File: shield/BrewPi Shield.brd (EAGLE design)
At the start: 53.6 x 59.7 mm, 31 parts, among them J1 ARDUINO_R3_SHIELD_ICSP, U1 SN74HC595N, U2 P-CHANNEL-MOSFET

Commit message: Version 1.2 upload
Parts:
- removed D1, D2: 1N4004, diode:DO41-10
- removed U2: P-CHANNEL-MOSFET, GeekAmmo:SOT23-3
- added Q1: 2N3906, transistor-pnp:TO92
- added R12: 10k Ohm, SparkFun-Passives:AXIAL-0.3
- R10: value 20-30 -> 220; device SparkFun-Passives:AXIAL-0.5 -> SparkFun-Passives:AXIAL-0.3
- R11: value 220 -> 470 Ohm
- RELAY: value 555 -> (none)
- moved R11 59.5 mm to (74.9, 25.4), turned to 270 degrees
- moved R10 56.6 mm to (36.8, 71.1), turned to 180 degrees
- moved R2 1.80 mm to (59.7, 44.5)
- moved R7 0.63 mm to (38.7, 33.0)
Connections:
- removed net N$10: LCD.15, R10.P$1
- removed net N$11: D1.A, U2.3
- removed net N$9: D2.C, R10.P$2
- new net N$7: Q1.1, R11.P$1
- net 5V: now also BTOOTH.4, Q1.3, R10.P$2; no longer BTOOTH.3, R11.P$2
- net A5V: no longer U2.2
- net GND: now also BTOOTH.3; no longer BTOOTH.4
- net N$13: now also R10.P$1; no longer R11.P$1
- net N$2: now also Q1.2, R12.P$2; no longer U1.2, U2.1
- net N$3: now also BTOOTH.1; no longer BTOOTH.2
- net N$5: now also LCD.15, R11.P$2; no longer D1.C, D2.A
- net QB: now also R12.P$1
- net RX: now also BTOOTH.2; no longer BTOOTH.1
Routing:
- net QB: track 10.7 -> 38.9 mm
- net N$9: track 22.3 -> 0.00 mm
- net N$2: track 24.6 -> 9.68 mm
- net A5V: track 60.8 -> 47.6 mm
- net N$11: track 12.0 -> 0.00 mm
- net 5V: track 175.0 -> 184.4 mm
- net N$10: track 9.20 -> 0.00 mm
- net RX: track 42.0 -> 45.5 mm
- net N$7: track 0.00 -> 3.44 mm
- net GND: track 200.7 -> 198.1 mm, vias 2 -> 1
- net SCK: track 44.4 -> 42.2 mm, vias 3 -> 2
- net N$5: track 10.8 -> 8.67 mm
- net N$1: track 5.08 -> 4.02 mm
- net SS: track 40.6 -> 39.6 mm
- net N$3: track 13.8 -> 14.7 mm
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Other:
- board text added: "BrewPi Shield v1.2"
- board text removed: "BrewPi Shield v1.1"

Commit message: Version 1.3 upload
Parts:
- removed BTOOTH: (no value), con-lstb:MA04-1
- removed LCD: 16 pin, pinhead:1X16
- removed LEDS: (no value), pinhead:1X02
- added ALARM, DOOR: 2 pin, LBussy:HEADER02-1
- added COOL_LED, HEAT_LED, ONE_WIRE_SEL: 3 pin, LBussy:HEADER03-1
- added I2C_LED, ROT_ENC, SERIAL: 4 pin, LBussy:HEADER04-1
- added PARALLEL_LCD_1, PARALLEL_LCD_2: 6 pin, LBussy:HEADER06-1
- added R13*: 10kΩ, SparkFun-Passives:AXIAL-0.3
- added RJ45: RJ45-8X, con-tycoelectronics:RJ45-NO-SHIELD
- C1, C2, C3, C4: value .1UF -> 0.1μF
- C5, C6, C7: value (none) -> 0.1μF
- C8: value 1.0UF -> 1.0μF
- PROBE1, PROBE2, PROBE3: value (none) -> 3 pin; device con-lstb:MA03-1 -> LBussy:HEADER03-1
- R1, R3, R4, R5: value 10K -> 10kΩ
- R10, R9: value 220 -> 220Ω
- R11: value 470 Ohm -> 150Ω
- R12: value 10k Ohm -> 10kΩ
- R2: value 0-20K -> 20kΩ
- R6: value 4.7K -> 4.7kΩ
- R7: value 1K -> 2kΩ
- R8: value 2K -> 1kΩ
- RELAY: value (none) -> 4 pin; device con-lstb:MA04-1 -> LBussy:HEADER04-1
- moved C1 43.0 mm to (62.7, 58.9), turned to 0 degrees
- moved R8 34.3 mm to (37.4, 63.5), turned to 180 degrees
- moved RELAY 33.1 mm to (37.4, 55.9)
- moved R7 32.9 mm to (37.4, 65.9)
- moved C2 28.8 mm to (37.4, 68.7), turned to 180 degrees
- moved C4 24.7 mm to (52.1, 21.5), turned to 180 degrees
- moved R9 15.9 mm to (48.9, 58.2)
- moved Q1 12.0 mm to (70.5, 22.2), turned to 0 degrees
- moved R10 12.0 mm to (48.9, 70.8)
- moved R5 11.3 mm to (37.4, 47.3), turned to 0 degrees
- moved C8 10.8 mm to (55.7, 74.9), turned to 90 degrees
- moved R4 8.64 mm to (37.4, 49.8), turned to 0 degrees
- moved C7 8.50 mm to (40.4, 37.3)
- moved C5 8.47 mm to (33.6, 37.3)
- moved C6 8.44 mm to (37.0, 37.3)
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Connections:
- removed net 5V: BTOOTH.4, C1.1, C2.1, J1.5V, LCD.2, PROBE1.2, PROBE2.2, PROBE3.2, Q1.3, R1.1, R10.P$2, R3.P$2, R4.P$2, R5.P$2, R6.P$1, R9.P$2, RELAY.3
- removed net A5V: C3.1, C4.1, C8.1, J1.5V_ICSP, R2.P$2, U1.16
- removed net AGND: C3.2, C4.2, C8.2, J1.GND_ICSP, U1.13, U1.8
- removed net D5: J1.D5, RELAY.2
- removed net D6: J1.D6, RELAY.1
- removed net D7: C5.1, J1.D7, R3.P$1
- removed net IO8: C6.1, J1.D8, R4.P$1
- removed net IO9: C7.1, J1.D9, R5.P$1
- removed net N$12: LEDS.1, R9.P$1
- removed net N$13: LEDS.2, R10.P$1
- new net 1WIRE: ONE_WIRE_SEL.2, PROBE1.3, PROBE2.3, PROBE3.3, R6.P$2, RJ45.4
- new net A0: J1.A0, ONE_WIRE_SEL.3
- new net A4: I2C_LED.3, J1.A4, ONE_WIRE_SEL.1
- new net A5: I2C_LED.4, J1.A5
- new net ALARM: ALARM.1, J1.D3
- new net COOL: J1.D5, R9.P$1, RELAY.2, RJ45.7
- new net DOOR: DOOR.1, J1.D4, RJ45.6
- new net HEAT: J1.D6, R10.P$2, RELAY.3, RJ45.8
- new net N$8: HEAT_LED.2, R10.P$1
- new net PSHB: C6.1, J1.D7, R4.P$1, ROT_ENC.2
- new net QC: R12.P$1, U1.2
- new net ROTA: C5.1, J1.D9, R3.P$1, ROT_ENC.1
- new net ROTB: C7.1, J1.D8, R5.P$1, ROT_ENC.4
- new net VCC: C1.1, C2.1, C3.1, C4.1, C8.1, COOL_LED.1, HEAT_LED.1, I2C_LED.2, J1.5V, J1.5V_ICSP, PARALLEL_LCD_1.2, PROBE1.2, PROBE2.2, PROBE3.2, Q1.3, R1.1, R2.P$2, R3.P$2, R4.P$2, R5.P$2, R6.P$1, RELAY.4, RJ45.3, SERIAL.4, U1.16
- net GND: now also ALARM.2, C3.2, C4.2, C8.2, COOL_LED.3, DOOR.2, HEAT_LED.3, I2C_LED.1, J1.GND_ICSP, PARALLEL_LCD_1.1, PARALLEL_LCD_1.5, PARALLEL_LCD_2.6, R13*.P$1, R7.P$1, RELAY.1, RJ45.5, ROT_ENC.3, SERIAL.3, U1.13, U1.8; no longer BTOOTH.3, LCD.1, LCD.16, LCD.5, R8.P$1, RELAY.4
- net N$2: now also R13*.P$2
- net N$3: now also R7.P$2, R8.P$1, SERIAL.1; no longer BTOOTH.1, R7.P$1, R8.P$2
- net N$4: now also COOL_LED.2, R9.P$2; no longer J1.A4, PROBE1.3, PROBE2.3, PROBE3.3, R6.P$2
- net N$5: now also PARALLEL_LCD_2.5; no longer LCD.15
- net N$6: now also PARALLEL_LCD_1.3; no longer LCD.3
- net QA: now also PARALLEL_LCD_1.4; no longer LCD.4
- net QB: now also PARALLEL_LCD_1.6; no longer LCD.6, R12.P$1
- net QE: now also PARALLEL_LCD_2.1; no longer LCD.11
- net QF: now also PARALLEL_LCD_2.2; no longer LCD.12
- net QG: now also PARALLEL_LCD_2.3; no longer LCD.13
- net QH: now also PARALLEL_LCD_2.4; no longer LCD.14
- net RX: now also SERIAL.2; no longer BTOOTH.2
- net TX: now also R8.P$2; no longer R7.P$2
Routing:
- net VCC: track 0.00 -> 239.9 mm, vias 0 -> 1
- net 5V: track 184.4 -> 0.00 mm, vias 2 -> 0
- net HEAT: track 0.00 -> 83.2 mm, vias 0 -> 4
- net COOL: track 0.00 -> 77.4 mm, vias 0 -> 1
- net GND: track 198.1 -> 261.7 mm
- net A4: track 0.00 -> 62.9 mm, vias 0 -> 1
- net 1WIRE: track 0.00 -> 62.0 mm
- net AGND: track 57.7 -> 0.00 mm
- net A5: track 0.00 -> 56.9 mm, vias 0 -> 2
- net DOOR: track 0.00 -> 49.5 mm
- net A5V: track 47.6 -> 0.00 mm
- net D5: track 45.3 -> 0.00 mm, vias 1 -> 0
- net D6: track 44.8 -> 0.00 mm, vias 1 -> 0
- net RX: track 45.5 -> 11.0 mm, vias 4 -> 0
- net TX: track 44.1 -> 10.5 mm, vias 2 -> 0
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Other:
- board text added: "11"
- board text added: "2"
- board text added: "3"
- board text added: "4"
- board text added: "5"
- board text added: "5 - GND 6 - DOOR 7 - COOL 8 - HEAT"
- board text added: "6"
- board text added: "7"
- board text added: "8"
- board text added: "A0"
- board text added: "A4"
- board text added: "BrewPi Remix I2C/RevC Shield @CadiBrewer v1.3 Inspired by @LBussy Based on a design by @day_trippr"
- board text added: "DAT"
- board text added: "ONE_WIRE"
- board text added: "PSH"
- board text added: "Q1"
- board text added: "RA"
- board text added: "RB"
- board text added: "RJ45 Pinout: 1 - 2 - 3 - VCC 4 - DATA"
- board text added: "SCL"
- board text added: "SDA"
- board text added: "https://www.brewpiremix.com"
- board text removed: "Based on a design by day_trippr on Homebrewtalk"
- board text removed: "BrewPi Shield v1.2"
- board text removed: "DATA"
- board text removed: "IN1"
- board text removed: "IN2"
- board text removed: "PROBES"
- board text removed: "by cadibrewer"

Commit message: Version 1.3.1 upload
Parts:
- removed R13*: 10kΩ, SparkFun-Passives:AXIAL-0.3
- added BACKLIGHT: 3 pin, LBussy:HEADER03-1
- moved R12 2.40 mm to (68.3, 33.4)
- moved R1 1.91 mm to (72.4, 29.8)
- moved R11 0.95 mm to (71.7, 26.4)
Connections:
- new net N$9: Q1.2, R12.P$2
- net GND: now also BACKLIGHT.1; no longer R13*.P$1
- net N$2: now also BACKLIGHT.2, R12.P$1; no longer Q1.2, R12.P$2, R13*.P$2
- net QC: now also BACKLIGHT.3; no longer R12.P$1
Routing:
- net N$2: track 19.4 -> 6.30 mm
- net GND: track 261.7 -> 272.8 mm, vias 1 -> 4
- net N$9: track 0.00 -> 9.95 mm
- net QC: track 17.6 -> 25.3 mm
- net QB: track 36.4 -> 33.1 mm, vias 2 -> 0
- net N$6: track 23.3 -> 20.5 mm
- net A5: track 56.9 -> 59.6 mm
- net N$7: track 6.66 -> 5.69 mm
- net VCC: track 239.9 -> 239.0 mm
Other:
- board text added: "BrewPi Remix I2C/RevC Shield @CadiBrewer v1.3.1 Inspired by @LBussy Based on a design by @day_trippr"
- board text added: "ON"
- board text added: "PB"
- board text removed: "BrewPi Remix I2C/RevC Shield @CadiBrewer v1.3 Inspired by @LBussy Based on a design by @day_trippr"

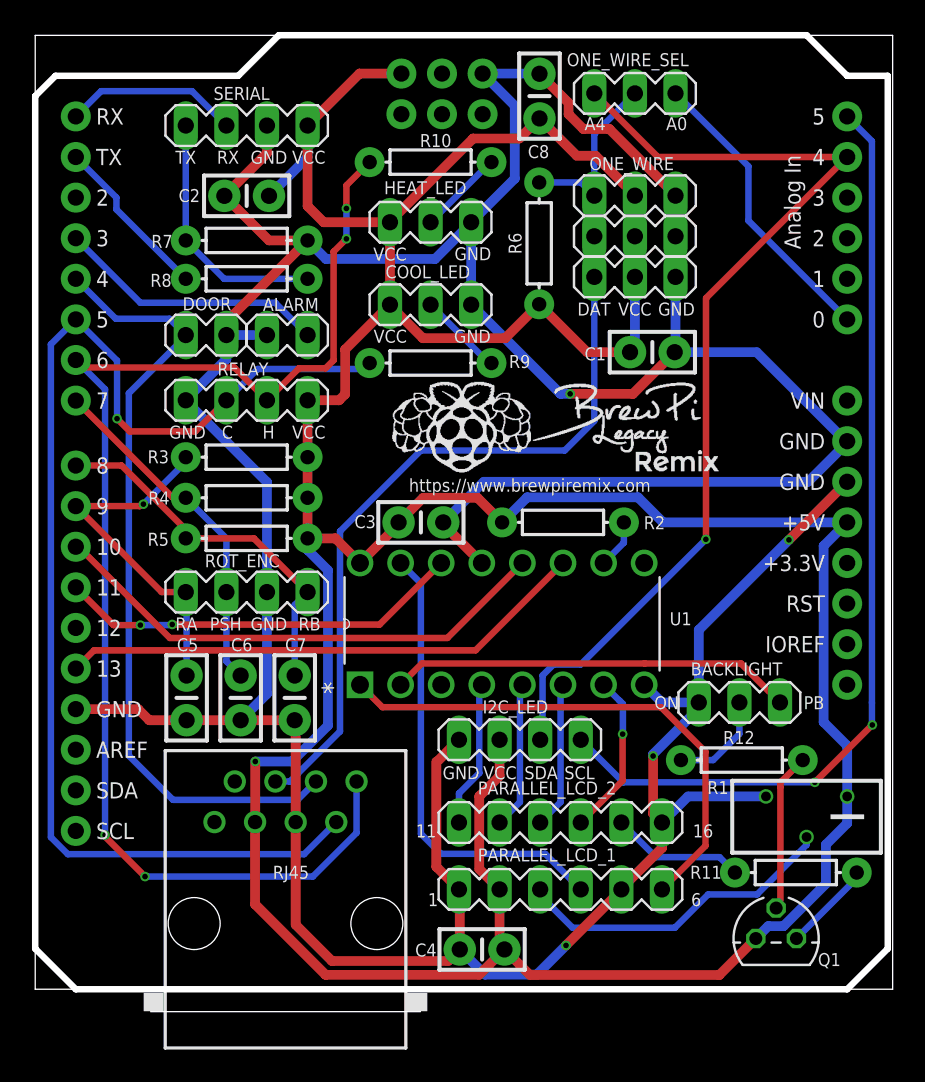
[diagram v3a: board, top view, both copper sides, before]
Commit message: Moved traces and silkscreens
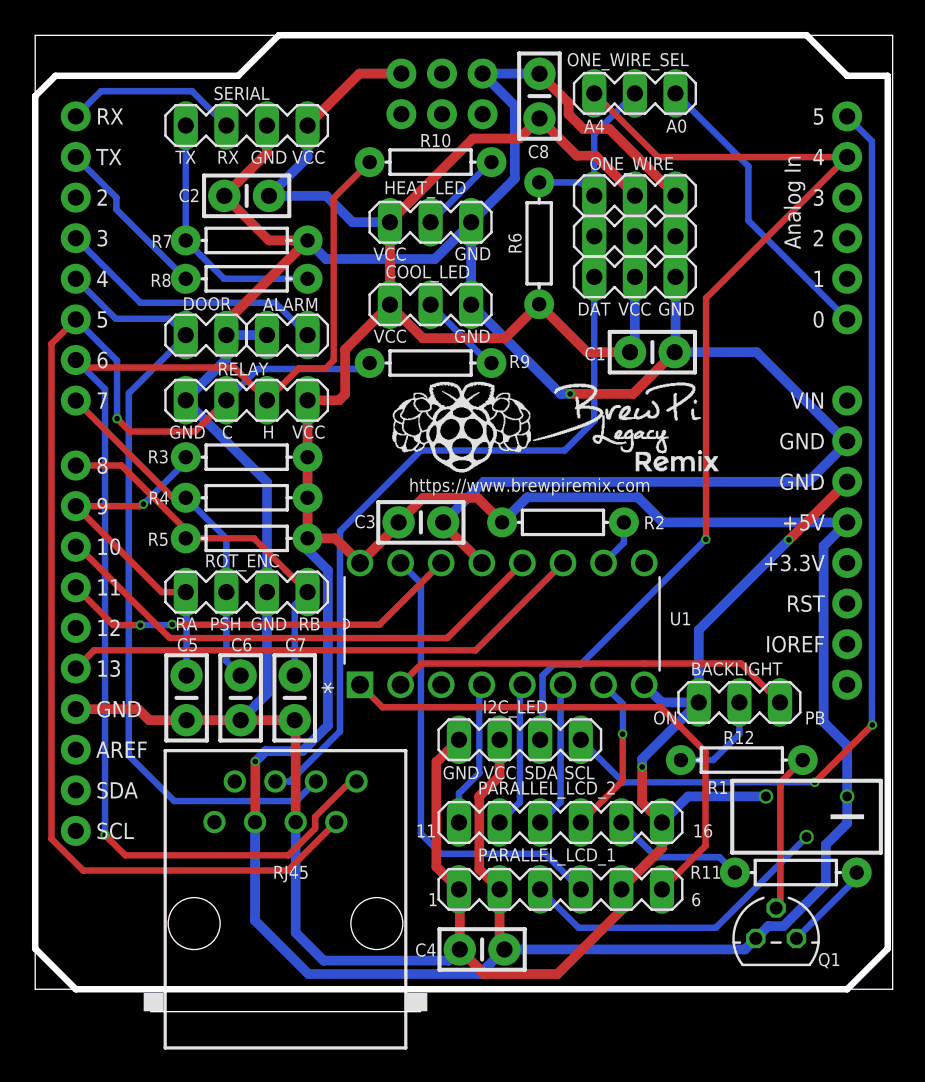
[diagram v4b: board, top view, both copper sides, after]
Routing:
- net VCC: track 239.0 -> 235.8 mm
- net HEAT: track 83.2 -> 80.6 mm, vias 4 -> 1
- net GND: track 272.8 -> 274.3 mm, vias 4 -> 3
- net COOL: track 77.4 -> 78.2 mm
- net N$6: track 20.5 -> 20.0 mm
